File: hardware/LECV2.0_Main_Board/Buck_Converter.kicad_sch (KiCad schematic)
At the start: 10 parts, among them U3 LMR33640ADDAR

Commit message: Added name to schematic
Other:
- company: (none) -> Missouri S&T Rocket Design Team
- title: (none) -> Buck_Converter_Schematic
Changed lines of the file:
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@@
 	(generator_version "9.0")
 	(paper "A4")
+	(title_block
+		(title "Buck_Converter_Schematic")
+		(date "2025-10-13")
+		(company "Missouri S&T Rocket Design Team")
+	)
 	(junction
 		(at 193.04 68.58)

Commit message: Temp commit to upload changes to buck converter circuit
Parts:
- added C10: 1u, Capacitor_SMD:C_0805_2012Metric, symbol Device:C
- added C12: DNP, Capacitor_SMD:C_0805_2012Metric, symbol Device:C
- added R8: 24.9K, Resistor_SMD:R_0603_1608Metric, symbol Device:R_US
- C5, C6, C7, C8: DigiKey https://www.digikey.com/en/products/detail/samsung-electro-mechanics/CL21A226MQQNNNE/3886758 -> https://www.digikey.com/en/products/detail/samsung-electro-mechanics/CL21A226MAYNNWE/16344162
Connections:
- net GND: now also C10.2, R8.2; no longer R6.1, U3.5 (FB)
- net Vout (5V): now also C12.2
- net at U3.6 (VCC): now also C10.1
- new net: C12.1, R6.1, R8.1, U3.5 (FB)
- no-connect marks 2 -> 1
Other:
- note added: "F_sw = 400kHz I_outMax = 4A"
- note added: "Optional 0805 footprint. Implement if output unstable."
- note added: "Voltage Divider to regulate FB to 1V."
- moved on the sheet: C5, L1, R6

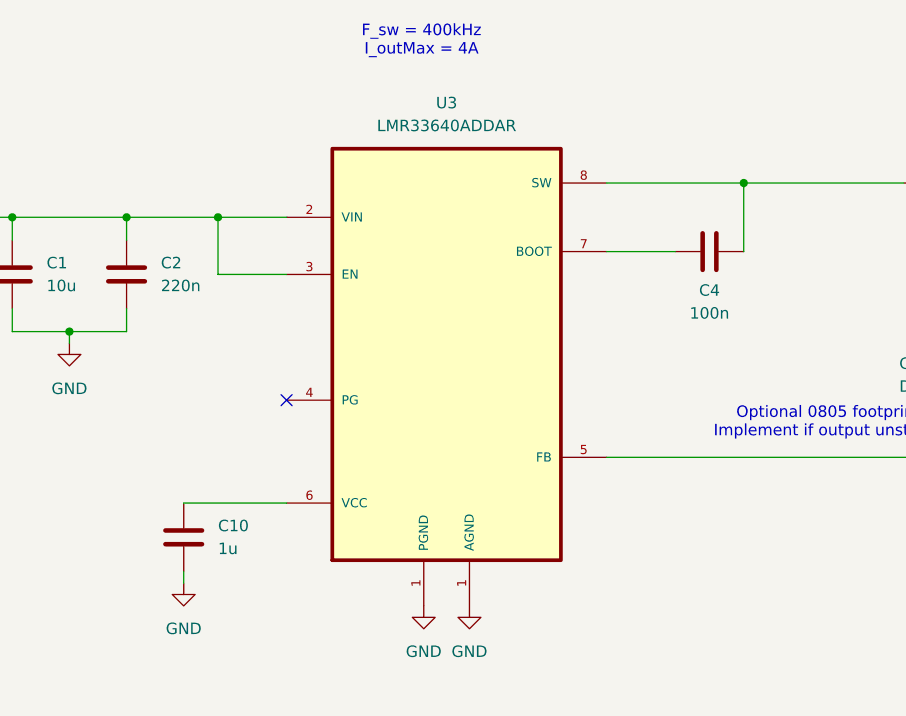
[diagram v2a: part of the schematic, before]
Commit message: Intermediate commit, need to fix servo connector footprints
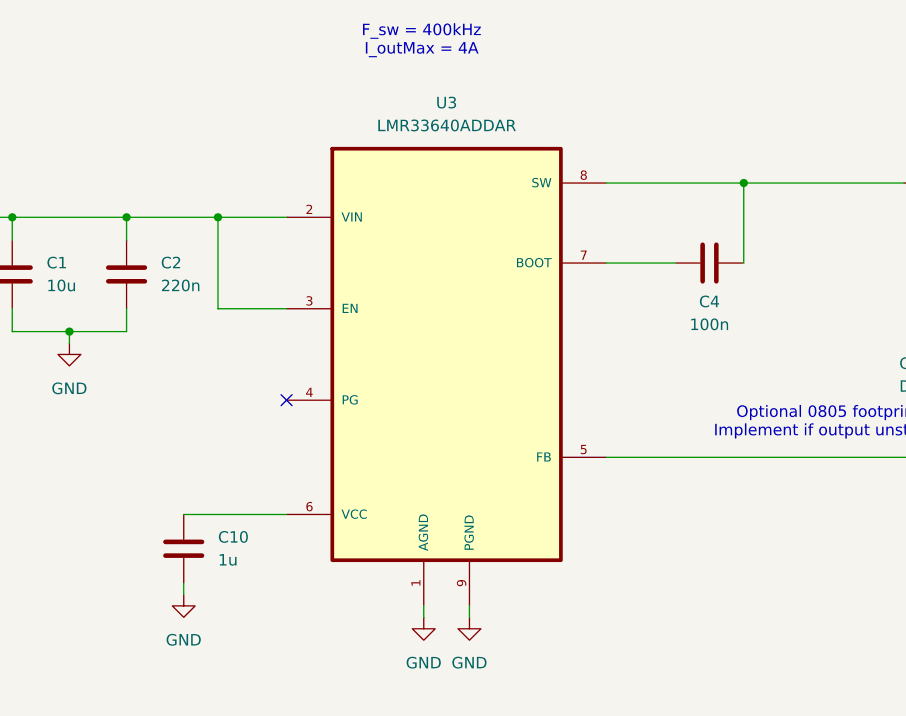
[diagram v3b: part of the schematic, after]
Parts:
- U3: footprint LMR33640ADDAR:VREG_LM5017MR_NOPB -> Package_SO:Texas_HSOP-8-1EP_3.9x4.9mm_P1.27mm_ThermalVias
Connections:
- net GND: now also U3.9 (PGND)
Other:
- moved on the sheet: C10, C4
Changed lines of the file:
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@@
 	(wire
 		(pts
-			(xy 140.97 68.58) (xy 140.97 76.2)
+			(xy 140.97 68.58) (xy 140.97 77.47)
+		)
+		(stroke
+			(width 0)
+			(type default)
+		)
+	)
+	(wire
+		(pts
+			(xy 110.49 116.84) (xy 110.49 115.57)
 		)
 		(stroke
@@
 	(wire
 		(pts
-			(xy 78.74 113.03) (xy 78.74 111.76)
+			(xy 78.74 114.3) (xy 78.74 113.03)
 		)
 		(stroke
@@
 	(wire
 		(pts
-			(xy 82.55 72.39) (xy 82.55 78.74)
+			(xy 82.55 72.39) (xy 82.55 82.55)
 		)
 		(stroke
@@
 	(wire
 		(pts
+			(xy 105.41 116.84) (xy 105.41 115.57)
+		)
+		(stroke
+			(width 0)
+			(type default)
+		)
+	)
+	(wire
+		(pts
 			(xy 125.73 99.06) (xy 167.64 99.06)
 		)
@@
 	(wire
 		(pts
-			(xy 78.74 104.14) (xy 90.17 104.14)
+			(xy 78.74 105.41) (xy 90.17 105.41)
 		)
 		(stroke
@@
 	(wire
 		(pts
-			(xy 82.55 78.74) (xy 90.17 78.74)
+			(xy 82.55 82.55) (xy 90.17 82.55)
 		)
 		(stroke
@@
 	(wire
 		(pts
-			(xy 125.73 76.2) (xy 133.35 76.2)
+			(xy 125.73 77.47) (xy 133.35 77.47)
 		)
 		(stroke
@@
 	(symbol
 		(lib_id "power:GND")
-		(at 105.41 115.57 0)
+		(at 105.41 116.84 0)
 		(unit 1)
 		(exclude_from_sim no)
@@
 		(fields_autoplaced yes)
 		(property "Reference" "#PWR038"
+			(at 105.41 123.19 0)
+			(effects
+				(font
+					(size 1.27 1.27)
+				)
+				(hide yes)
+			)
+		)
+		(property "Value" "GND"
 			(at 105.41 121.92 0)
 			(effects
@@
 					(size 1.27 1.27)
 				)
-				(hide yes)
-			)
-		)
-		(property "Value" "GND"
-			(at 105.41 120.65 0)
-			(effects
-				(font
-					(size 1.27 1.27)
-				)
 			)
 		)
 		(property "Footprint" ""
-			(at 105.41 115.57 0)
+			(at 105.41 116.84 0)
 			(effects
 				(font
@@
 		)
 		(property "Datasheet" ""
-			(at 105.41 115.57 0)
+			(at 105.41 116.84 0)
 			(effects
 				(font
@@
 		)
 		(property "Description" "Power symbol creates a global label with name \"GND\" , ground"
-			(at 105.41 115.57 0)
+			(at 105.41 116.84 0)
 			(effects
 				(font
@@
 	(symbol
 		(lib_id "power:GND")
-		(at 78.74 113.03 0)
+		(at 78.74 114.3 0)
 		(unit 1)
 		(exclude_from_sim no)
@@
 		(fields_autoplaced yes)
 		(property "Reference" "#PWR026"
+			(at 78.74 120.65 0)
+			(effects
+				(font
+					(size 1.27 1.27)
+				)
+				(hide yes)
+			)
+		)
+		(property "Value" "GND"
 			(at 78.74 119.38 0)
 			(effects
@@
 					(size 1.27 1.27)
 				)
-				(hide yes)
-			)
-		)
-		(property "Value" "GND"
-			(at 78.74 118.11 0)
-			(effects
-				(font
-					(size 1.27 1.27)
-				)
 			)
 		)
 		(property "Footprint" ""
-			(at 78.74 113.03 0)
+			(at 78.74 114.3 0)
 			(effects
 				(font
@@
 		)
 		(property "Datasheet" ""
-			(at 78.74 113.03 0)
+			(at 78.74 114.3 0)
 			(effects
 				(font
@@
 		)
 		(property "Description" "Power symbol creates a global label with name \"GND\" , ground"
-			(at 78.74 113.03 0)
+			(at 78.74 114.3 0)
 			(effects
 				(font
@@
 	(symbol
 		(lib_id "Device:C")
-		(at 78.74 107.95 0)
+		(at 78.74 109.22 0)
 		(unit 1)
 		(exclude_from_sim no)
@@
 		(dnp no)
 		(property "Reference" "C10"
-			(at 82.55 106.68 0)
+			(at 82.55 107.95 0)
 			(effects
 				(font
@@
 		)
 		(property "Value" "1u"
-			(at 82.55 109.22 0)
+			(at 82.55 110.49 0)
 			(effects
 				(font
@@
 		)
 		(property "Footprint" "Capacitor_SMD:C_0805_2012Metric"
-			(at 79.7052 111.76 0)
+			(at 79.7052 113.03 0)
 			(effects
 				(font
@@
 		)
 		(property "Datasheet" "https://mm.digikey.com/Volume0/opasdata/d220001/medias/docus/3713/CL21Y105KCYVPNE_DS.pdf"
-			(at 78.74 107.95 0)
+			(at 78.74 109.22 0)
 			(effects
 				(font
@@
 		)
 		(property "Description" ""
-			(at 78.74 107.95 0)
+			(at 78.74 109.22 0)
 			(effects
 				(font
@@
 		)
 		(property "DigiKey" "https://www.digikey.com/en/products/detail/samsung-electro-mechanics/CL21Y105KCYVPNE/14565404"
-			(at 78.74 107.95 0)
+			(at 78.74 109.22 0)
 			(effects
 				(font
@@
 	(symbol
 		(lib_id "Device:C")
-		(at 137.16 76.2 90)
+		(at 137.16 77.47 90)
 		(unit 1)
 		(exclude_from_sim no)
@@
 		(dnp no)
 		(property "Reference" "C4"
-			(at 137.16 80.518 90)
+			(at 137.16 81.788 90)
 			(effects
 				(font
@@
 		)
 		(property "Value" "100n"
-			(at 137.16 83.058 90)
+			(at 137.16 84.328 90)
 			(effects
 				(font
@@
 		)
 		(property "Footprint" "Capacitor_SMD:C_0603_1608Metric"
-			(at 140.97 75.2348 0)
+			(at 140.97 76.5048 0)
 			(effects
 				(font
@@
 		)
 		(property "Datasheet" "https://mm.digikey.com/Volume0/opasdata/d220001/medias/docus/609/CL10B104KB8NNNC_Spec.pdf"
-			(at 137.16 76.2 0)
+			(at 137.16 77.47 0)
 			(effects
 				(font
@@
 		)
 		(property "Description" ""
-			(at 137.16 76.2 0)
+			(at 137.16 77.47 0)
 			(effects
 				(font
@@
 		)
 		(property "DigiKey" "https://www.digikey.com/en/products/detail/samsung-electro-mechanics/CL10B104KB8NNNC/3886658"
-			(at 137.16 76.2 0)
+			(at 137.16 77.47 0)
 			(effects
 				(font
@@
 	(symbol
 		(lib_id "power:GND")
-		(at 110.49 115.57 0)
+		(at 110.49 116.84 0)
 		(unit 1)
 		(exclude_from_sim no)
@@
 		(fields_autoplaced yes)
 		(property "Reference" "#PWR037"
+			(at 110.49 123.19 0)
+			(effects
+				(font
+					(size 1.27 1.27)
+				)
+				(hide yes)
+			)
+		)
+		(property "Value" "GND"
 			(at 110.49 121.92 0)
 			(effects
@@
 					(size 1.27 1.27)
 				)
-				(hide yes)
-			)
-		)
-		(property "Value" "GND"
-			(at 110.49 120.65 0)
-			(effects
-				(font
-					(size 1.27 1.27)
-				)
 			)
 		)
 		(property "Footprint" ""
-			(at 110.49 115.57 0)
+			(at 110.49 116.84 0)
 			(effects
 				(font
@@
 		)
 		(property "Datasheet" ""
-			(at 110.49 115.57 0)
+			(at 110.49 116.84 0)
 			(effects
 				(font
@@
 		)
 		(property "Description" "Power symbol creates a global label with name \"GND\" , ground"
-			(at 110.49 115.57 0)
+			(at 110.49 116.84 0)
 			(effects
 				(font
@@
 			)
 		)
-		(property "Footprint" "LMR33640ADDAR:VREG_LM5017MR_NOPB"
+		(property "Footprint" "Package_SO:Texas_HSOP-8-1EP_3.9x4.9mm_P1.27mm_ThermalVias"
 			(at 107.95 87.63 0)
 			(effects
@@
 		(pin "8"
 		)
-		(pin "1"
+		(pin "9"
 		)
 		(pin "6"

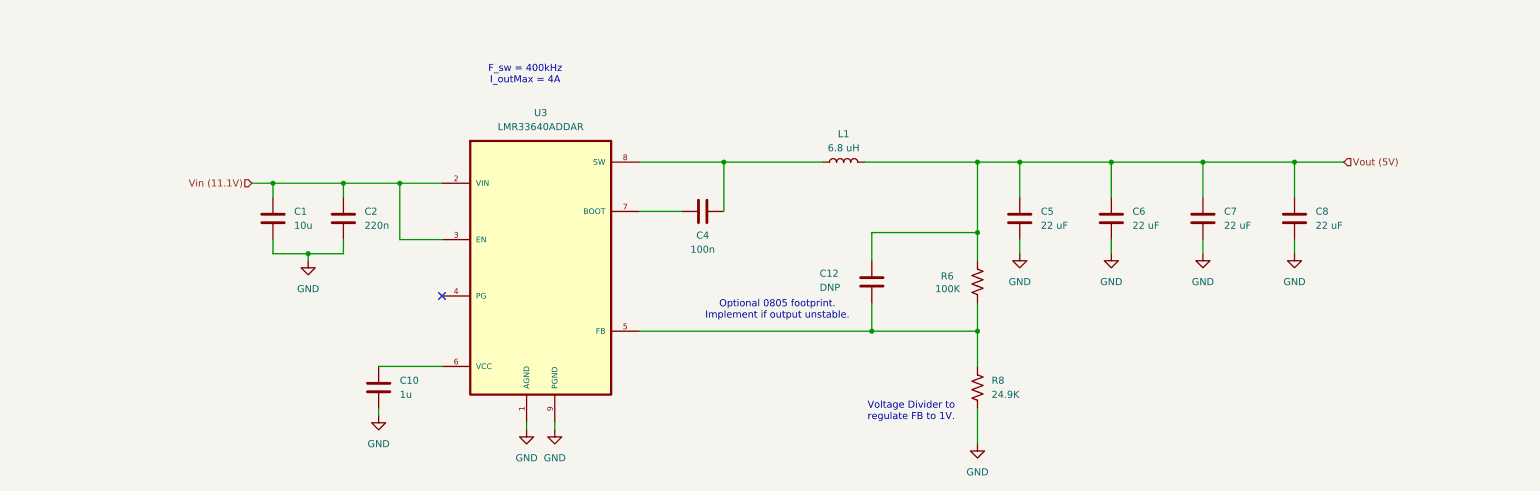
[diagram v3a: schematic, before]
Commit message: Added GPIO clamping diodes, sufficient buck output capacitance, UVLO divider, and 3V3_EN diode
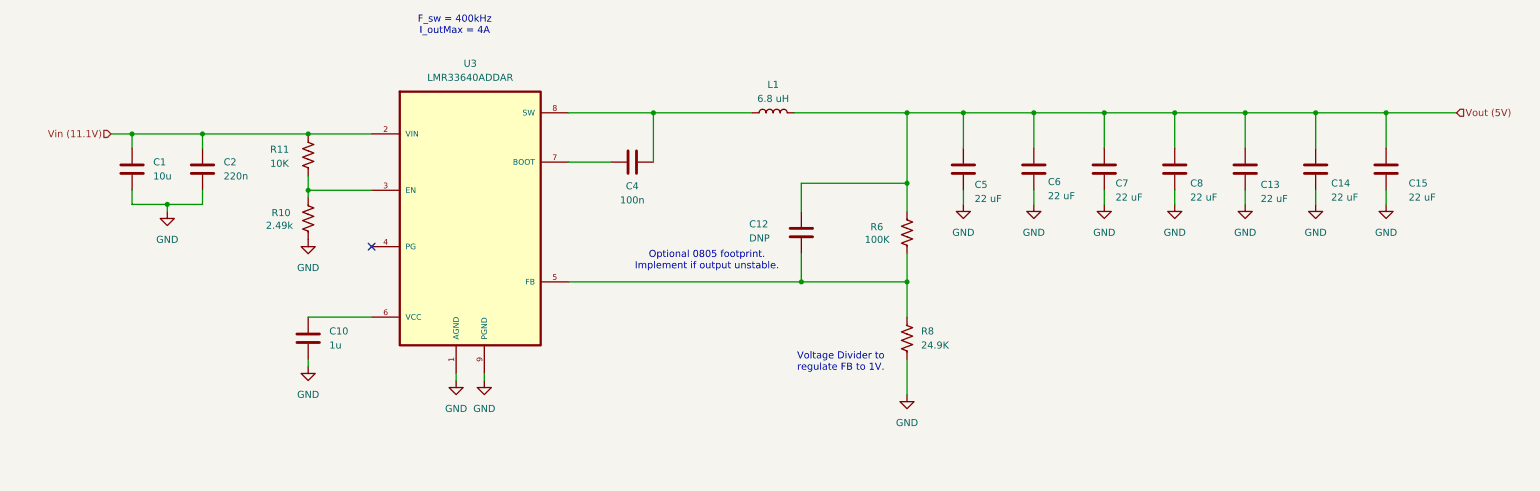
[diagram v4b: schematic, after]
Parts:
- added C13, C14, C15: 22 uF, Capacitor_SMD:C_0805_2012Metric, symbol Device:C
- added R10: 2.49k, Resistor_SMD:R_0603_1608Metric, symbol Device:R_US
- added R11: 10K, Resistor_SMD:R_0603_1608Metric, symbol Device:R_US
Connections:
- net GND: now also C13.2, C14.2, C15.2, R10.1
- net Vin (11.1V): now also R11.1; no longer U3.3 (EN)
- net Vout (5V): now also C13.1, C14.1, C15.1
- new net: R10.2, R11.2, U3.3 (EN)
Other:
- moved on the sheet: C1, C10, C12, C2, C4, C5, C6, C7, C8, L1, R6, R8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

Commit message: Finished PCBs
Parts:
- added C19: 10u, Capacitor_SMD:C_1210_3225Metric, symbol Device:C
- C1: footprint Capacitor_SMD:C_0805_2012Metric -> Capacitor_SMD:C_1210_3225Metric; DigiKey https://www.digikey.com/en/products/detail/samsung-electro-mechanics/CL21A106KAYNNNE/3888549 -> https://www.digikey.com/en/products/detail/samsung-electro-mechanics/CL32B106KBJNNNE/3889045
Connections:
- net GND: now also C19.2
- net Vin (11.1V): now also C19.1
- net SW: now reaches C4.2, L1.1, U3.8 (SW)
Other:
- moved on the sheet: C1, C10, C2, R10, R11, U3
